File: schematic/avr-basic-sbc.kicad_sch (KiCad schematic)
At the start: 32 parts, among them J1 DC-005 Power Jack, J2 PS/2 keyboard port, J3 RCA Video Jack, J4 Port B, J5 Port A, J6 Port C, J7 Port D, J8 USBasp header, J9 Power output header, U1 ATmega1284P-P, U2 L7805, U3 25LC640, Y1 16 MHz

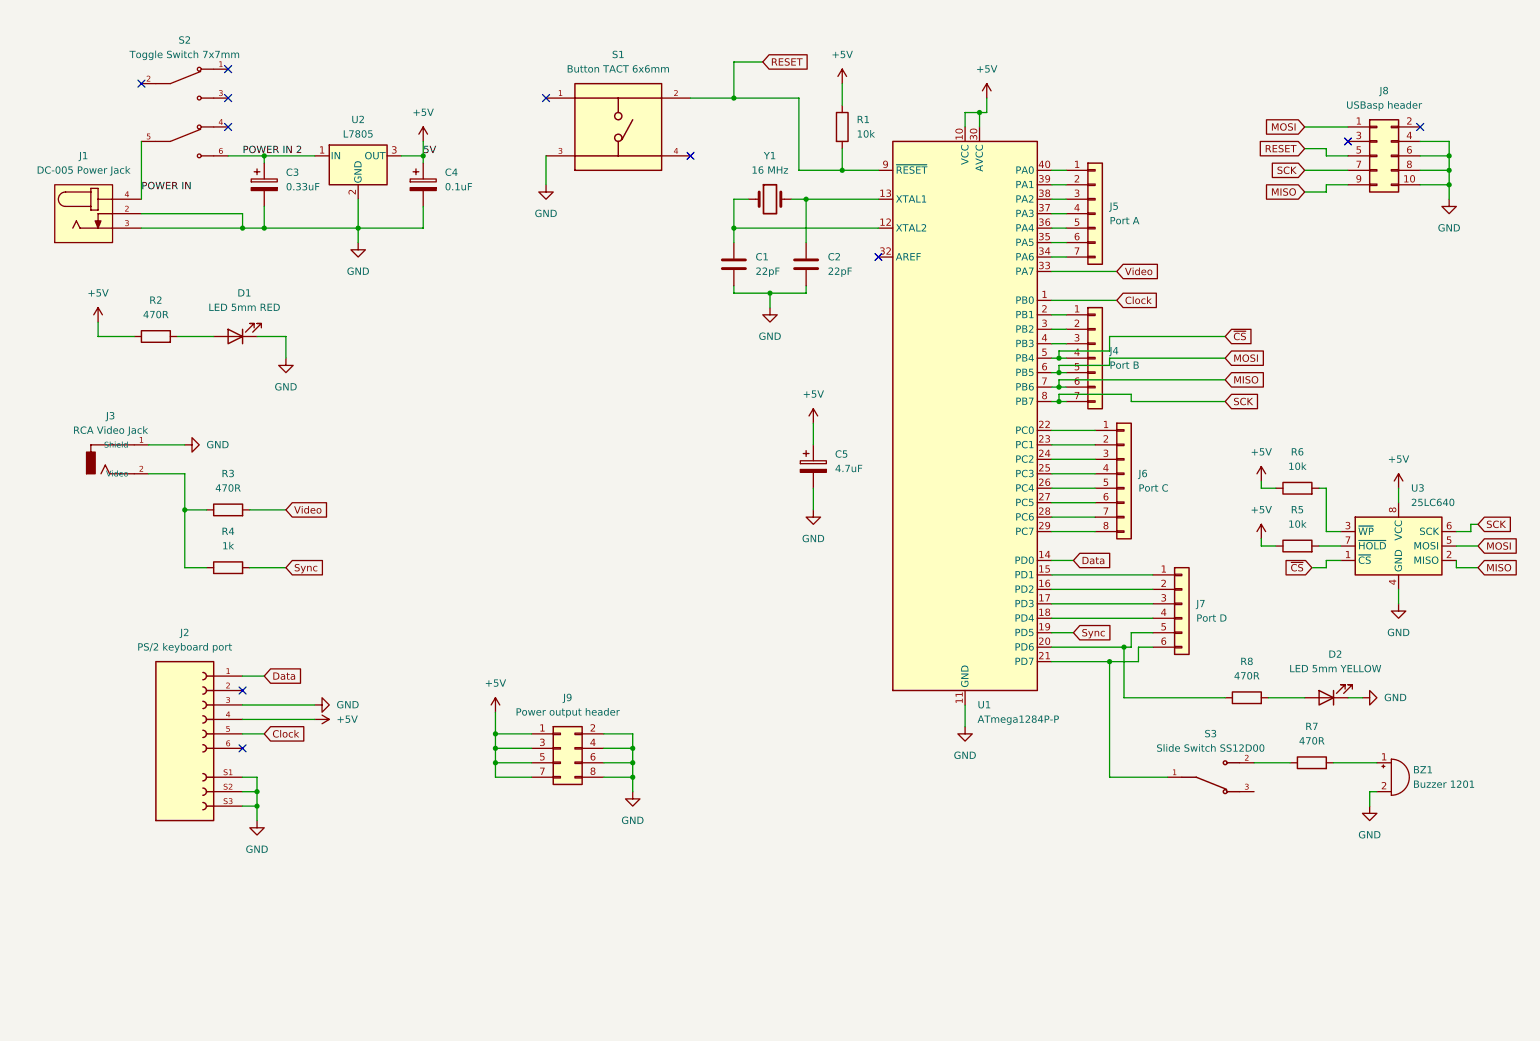
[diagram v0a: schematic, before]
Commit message: AVR-SBC board schematic rearranged to make it look nicer, PDF regenerated
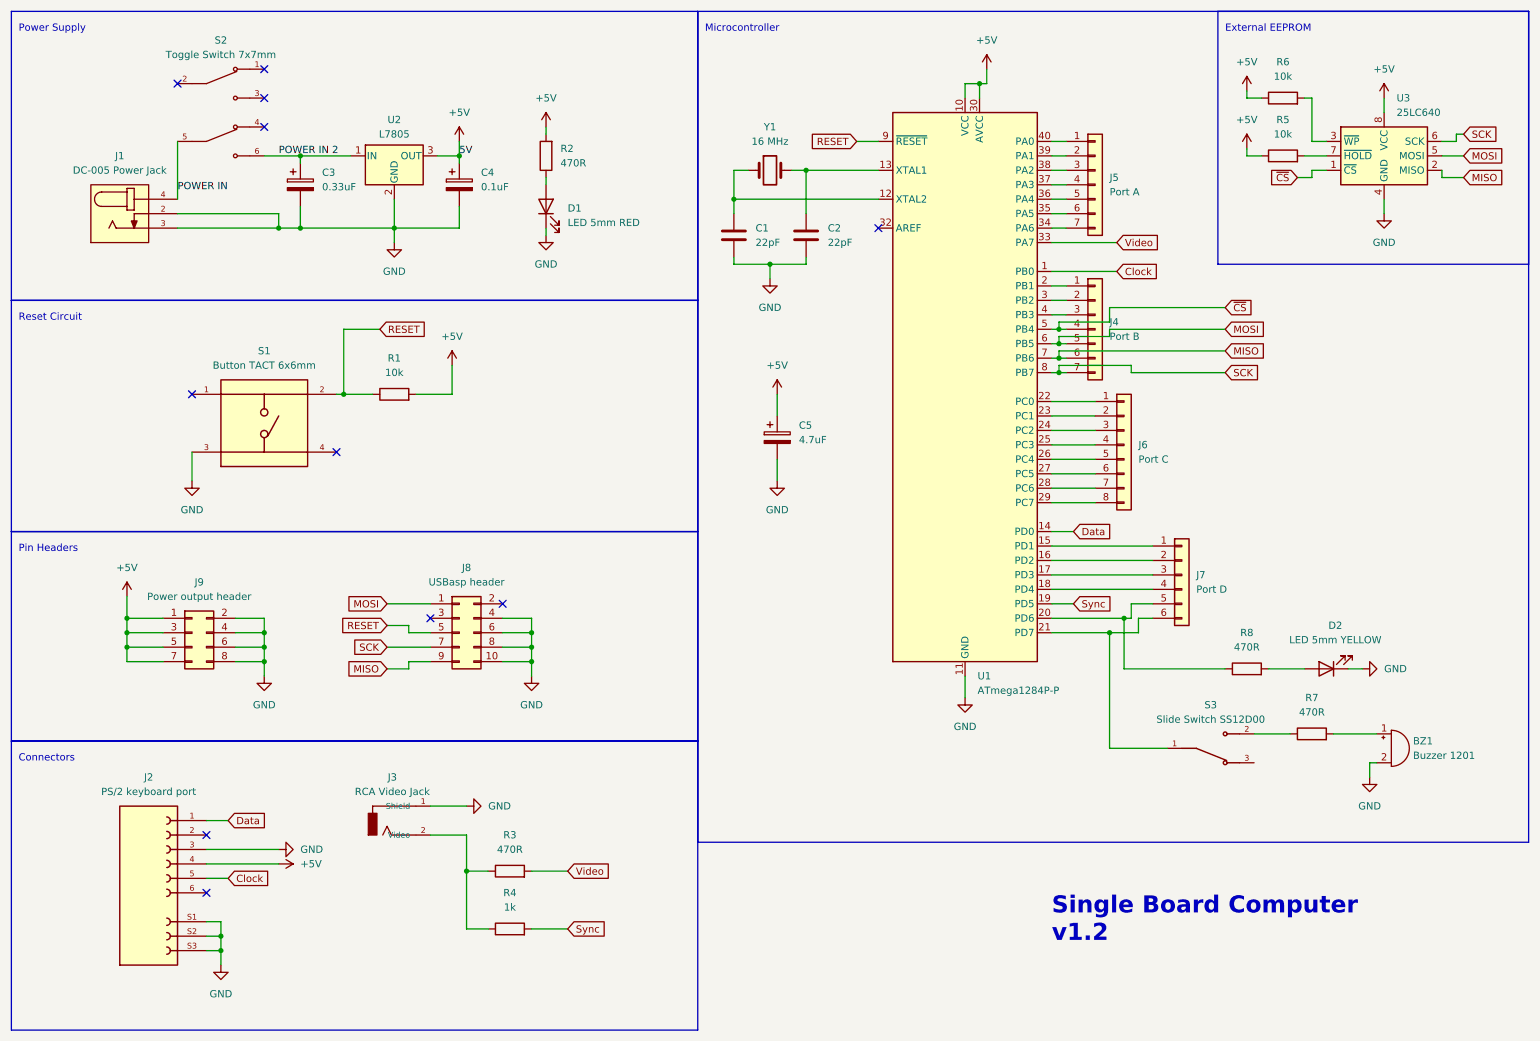
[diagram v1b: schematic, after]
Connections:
- net +5V: now also R1.2, R2.2; no longer R1.1, R2.1
- net RESET: now also R1.1; no longer R1.2
- net at D1.2 (A): now also R2.1; no longer R2.2
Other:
- note added: "Connectors"
- note added: "External EEPROM"
- note added: "Microcontroller"
- note added: "Pin Headers"
- note added: "Power Supply"
- note added: "Reset Circuit"
- note added: "Single Board Computer v1.2"
- title: ATMEGA1284P Single Board Computer -> AVR-SBC ATMEGA1284P Single Board Computer
- moved on the sheet: BZ1, C1, C2, C3, C4, C5, D1, D2, J1, J2, J3, J4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

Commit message: Schematic: Update to v1.3, schottky diode added to ISP header for protection, decoupling capacitors added
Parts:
- added C2: 0.33uF, StockLib:C_100nF_L7.0mm_W2.5mm_P5.00mm, symbol Device:C
- added C3, C8, C9: 0.1uF, StockLib:C_100nF_L7.0mm_W2.5mm_P5.00mm, symbol Device:C
- added D1: 1N4001, Diode_THT:D_DO-41_SOD81_P10.16mm_Horizontal, symbol Diode:1N4001
- added D4: 1N5819, Diode_THT:D_DO-41_SOD81_P10.16mm_Horizontal, symbol StockLib:1N5819
- C1: renamed from C3; value 0.33uF -> 10uF; footprint Capacitor_THT:CP_Radial_D6.3mm_P2.50mm -> Capacitor_THT:CP_Radial_D5.0mm_P2.00mm
- C4: value 0.1uF -> 10uF; footprint Capacitor_THT:CP_Radial_D6.3mm_P2.50mm -> Capacitor_THT:CP_Radial_D5.0mm_P2.00mm
- C7: renamed from C5; footprint Capacitor_THT:CP_Radial_D6.3mm_P2.50mm -> Capacitor_THT:CP_Radial_D5.0mm_P2.00mm
- renumbered C1 to C5, C2 to C6, D1 to D2, D2 to D3, J9 to J3, J3 to J4, J8 to J5, J5 to J6, J4 to J7, J6 to J8, J7 to J9, R3 to R2, R4 to R3, R2 to R4, R8 to R5, R5 to R7, R7 to R8, U2 to U1, U1 to U2
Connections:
- net +5V: now also C3.2, C8.2, C9.2, D1.2 (A), D4.1 (K)
- net GND: now also C2.1, C3.1, C8.1, C9.1
- net POWER IN 2: now also C2.2, D1.1 (K)
- net at J5.2 (Pin_2): now also D4.2 (A)
- no-connect marks 11 -> 10
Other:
- note added: "Power LED"
- note added: "Single Board Computer v1.3"
- note removed: "Single Board Computer v1.2"
- moved on the sheet: C1, C4, C7, D2, J1, R1, R4, S1, S2, U1

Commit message: PCB reverted to release version v1.2
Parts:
- removed C2: 0.33uF, StockLib:C_100nF_L7.0mm_W2.5mm_P5.00mm, symbol Device:C
- removed C3, C8, C9: 0.1uF, StockLib:C_100nF_L7.0mm_W2.5mm_P5.00mm, symbol Device:C
- removed D1: 1N4001, Diode_THT:D_DO-41_SOD81_P10.16mm_Horizontal, symbol Diode:1N4001
- removed D4: 1N5819, Diode_THT:D_DO-41_SOD81_P10.16mm_Horizontal, symbol StockLib:1N5819
- C3: renamed from C1; value 10uF -> 0.33uF; footprint Capacitor_THT:CP_Radial_D5.0mm_P2.00mm -> Capacitor_THT:CP_Radial_D6.3mm_P2.50mm
- C4: value 10uF -> 0.1uF; footprint Capacitor_THT:CP_Radial_D5.0mm_P2.00mm -> Capacitor_THT:CP_Radial_D6.3mm_P2.50mm
- C5: renamed from C7; footprint Capacitor_THT:CP_Radial_D5.0mm_P2.00mm -> Capacitor_THT:CP_Radial_D6.3mm_P2.50mm
- renumbered C5 to C1, C6 to C2, D2 to D1, D3 to D2, J4 to J3, J7 to J4, J6 to J5, J8 to J6, J9 to J7, J5 to J8, J3 to J9, R4 to R2, R2 to R3, R3 to R4, R7 to R5, R8 to R7, R5 to R8, U2 to U1, U1 to U2
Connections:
- no-connect marks 10 -> 11
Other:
- note added: "Single Board Computer v1.2"
- note removed: "Power LED"
- note removed: "Single Board Computer v1.3"
- moved on the sheet: C3, C4, C5, D1, J1, R1, R2, S1, S2, U2

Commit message: Schematic migrated to KiCad 9, image added to docs/images
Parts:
- C3: value 0.33uF -> 3.3uF
- C4: value 0.1uF -> 1uF
